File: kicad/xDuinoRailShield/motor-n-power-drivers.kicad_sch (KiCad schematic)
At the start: 3 parts, among them U5 ULN2003A, U6 ULN2003A, U8 DRV8872DDA

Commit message: More busses added
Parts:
- removed U6: ULN2003A, symbol Transistor_Array:ULN2003A
- renumbered U5 to U901, U8 to U902
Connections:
- net AUX1_AMP renamed AMP_AUX1
- net AUX2_AMP renamed AMP_AUX2
- net AUX3_AMP renamed AMP_AUX3
- net AUX4_AMP renamed AMP_AUX4
- net AUX5_AMP renamed AMP_AUX5
- net F0_BACKWARD renamed F01
- net F0_BACKWARD_AMP renamed AMP_F01
- net F0_FRONTWARD renamed F00
- net F0_FRONTWARD_AMP renamed AMP_F00
- net MOTOR+ renamed AMP_MOTOR0
- net MOTOR- renamed AMP_MOTOR1
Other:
- moved on the sheet: U901, U902

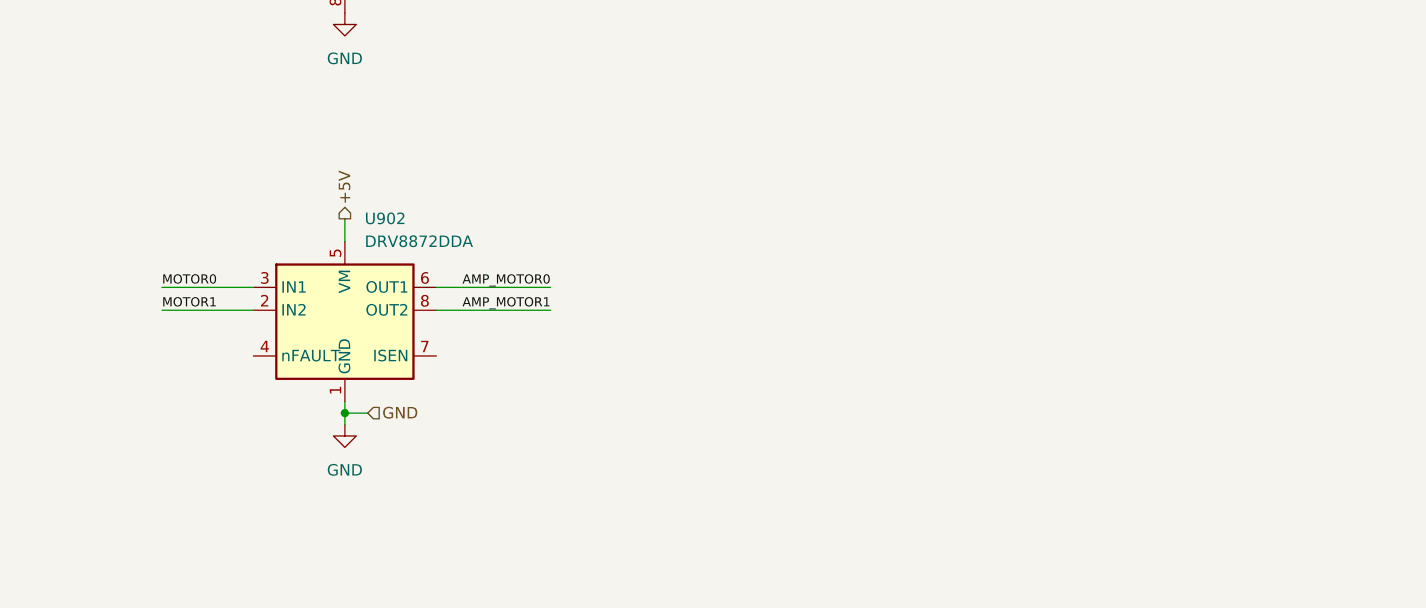
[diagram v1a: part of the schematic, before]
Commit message: Draft of loco decoder
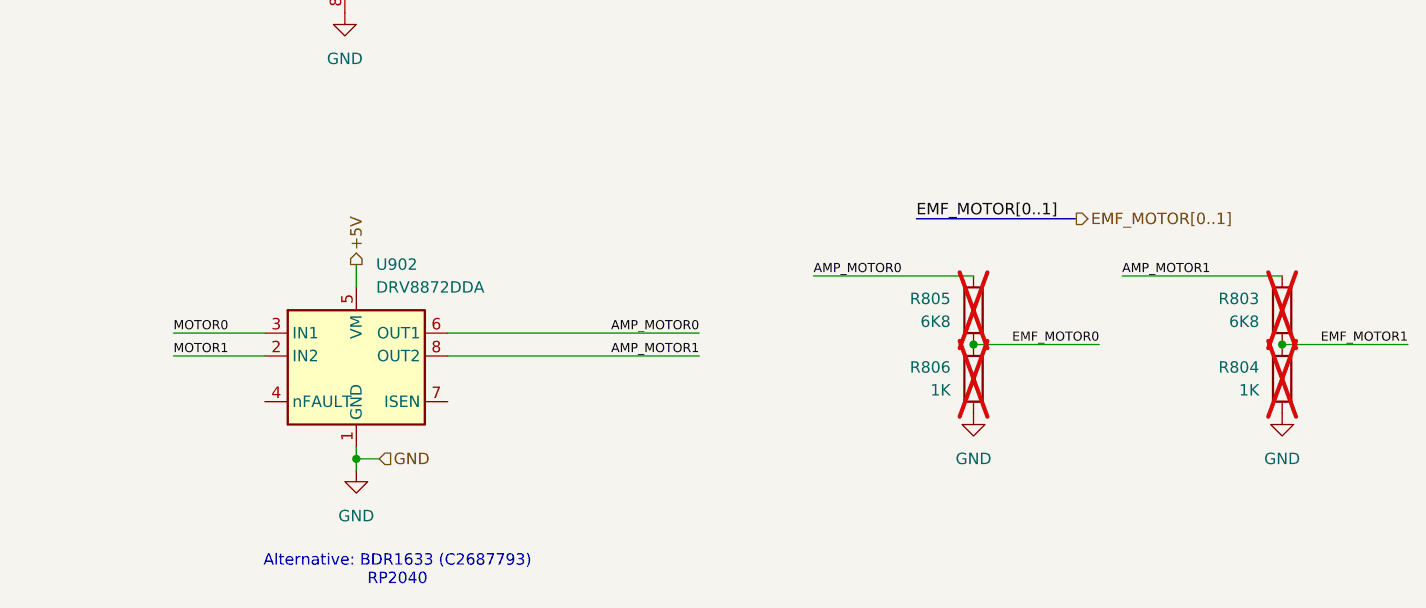
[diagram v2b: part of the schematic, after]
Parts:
- added R803, R805: 6K8, Resistor_SMD:R_0805_2012Metric_Pad1.20x1.40mm_HandSolder, symbol Device:R
- added R804, R806: 1K, Resistor_SMD:R_0805_2012Metric_Pad1.20x1.40mm_HandSolder, symbol Device:R
- U901: footprint (none) -> Package_SO:SOIC-16_4.55x10.3mm_P1.27mm; LCSC (none) -> C7512
- U902: LCSC (none) -> C114179
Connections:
- net AMP_MOTOR0: now also R805.1
- net AMP_MOTOR1: now also R803.1
- net GND: now also R804.2, R806.2
- new net EMF_MOTOR0: R805.2, R806.1
- new net EMF_MOTOR1: R803.2, R804.1
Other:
- note added: "Alternative: BDR1633 (C2687793) RP2040"
- moved on the sheet: U902

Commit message: A lot of fixes
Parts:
- removed U902: DRV8872DDA, Package_SO:Texas_HTSOP-8-1EP_3.9x4.9mm_P1.27mm_EP2.95x4.9mm_Mask2.4x3.1mm_ThermalVias, symbol Driver_Motor:DRV8872DDA
- added U801: BDR6133, BDR6133:BDR6133, symbol BDR6133:BDR6133
- added U802: DRV8872DDA, Package_SO:Texas_HTSOP-8-1EP_3.9x4.9mm_P1.27mm_EP2.95x4.9mm_Mask2.4x3.1mm_ThermalVias, symbol Driver_Motor:DRV8872DDA
- added U804: ULN2003A, Package_SO:SOIC-16_4.55x10.3mm_P1.27mm, symbol Transistor_Array:ULN2003A
- renumbered R805 to R801, R806 to R802, U901 to U803
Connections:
- net +5V: now also U801.2 (VCC), U802.5 (VM)
- net AMP_AUX2: no longer U803.13 (O4)
- net AMP_AUX3: no longer U803.12 (O5)
- net AMP_AUX4: no longer U803.11 (O6)
- net AMP_AUX5: no longer U803.10 (O7)
- net AMP_MOTOR0: now also U801.4 (OUTA), U802.6 (OUT1)
- net AMP_MOTOR1: now also U801.5 (OUTB), U802.8 (OUT2)
- net AUX2: no longer U803.4 (I4)
- net AUX3: no longer U803.5 (I5)
- net AUX4: no longer U803.6 (I6)
- net AUX5: no longer U803.7 (I7)
- net GND: now also U801.1 (GND), U802.1 (GND), U802.9 (GND), U804.8 (GND)
- net MOTOR0: now also U801.6 (INA), U802.3 (IN1)
- net MOTOR1: now also U801.7 (INB), U802.2 (IN2)
- net AMP_F00 renamed AMP_FUNC0
- net AMP_F01 renamed AMP_FUNC1
- net F00 renamed FUNC0
- net F01 renamed FUNC1
- new net AMP_AUX6: U804.16 (O1)
- new net AMP_AUX7: U804.15 (O2)
- new net AMP_AUX8: U804.14 (O3)
- new net AUX6: U804.1 (I1)
- new net AUX7: U804.2 (I2)
- new net AUX8: U804.3 (I3)
- new net U+: U801.3 (VM)
- no-connect marks 0 -> 28
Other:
- note added: "Motor Driver"
- note added: "Output Driver"
- note removed: "Alternative: BDR1633 (C2687793) RP2040"
- moved on the sheet: R801, R802, R803, R804, U803

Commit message: Final version
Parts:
- R801, R802, R803, R804: now fitted; now in the parts list
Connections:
- net AMP_AUX1: now also U803.15 (O2); no longer U803.14 (O3)
- net AMP_FUNC1: now also U803.14 (O3); no longer U803.15 (O2)
- net AUX1: now also U803.2 (I2); no longer U803.3 (I3)
- net FUNC1: now also U803.3 (I3); no longer U803.2 (I2)

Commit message: Refactoring & Sound
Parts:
- added Q801, Q802, Q803, Q804: 2N7002, Package_TO_SOT_SMD:SOT-23, symbol Transistor_FET:2N7002
- R801, R802, R803, R804: footprint Resistor_SMD:R_0805_2012Metric_Pad1.20x1.40mm_HandSolder -> Resistor_SMD:R_0402_1005Metric_Pad0.72x0.64mm_HandSolder
- U803: now not fitted; now left out of the parts list
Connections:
- net AMP_AUX1: now also Q803.3 (D)
- net AMP_AUX2: now also Q804.3 (D)
- net AMP_FUNC0: now also Q801.3 (D)
- net AMP_FUNC1: now also Q802.3 (D)
- net AUX1: now also Q803.1 (G)
- net AUX2: now also Q804.1 (G)
- net FUNC0: now also Q801.1 (G)
- net FUNC1: now also Q802.1 (G)
- net GND: now also Q801.2 (S), Q802.2 (S), Q803.2 (S), Q804.2 (S)

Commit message: More refactoring
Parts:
- Q801, Q802, Q803: LCSC (none) -> C8545
- R801, R803: value 6K8 -> 10k; LCSC C17772 -> C25744
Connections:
- net U+: now also U802.5 (VM)
- net +5V renamed +3V3
- net +3V3: no longer U802.5 (VM)
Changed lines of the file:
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@@
 	(wire
 		(pts
-			(xy 97.79 33.02) (xy 97.79 38.1)
+			(xy 97.79 31.75) (xy 97.79 38.1)
 		)
 		(stroke
@@
 		)
 	)
-	(hierarchical_label "+5V"
+	(hierarchical_label "+3V3"
 		(shape input)
 		(at 43.18 33.02 90)
@@
 		)
 	)
-	(hierarchical_label "+5V"
+	(hierarchical_label "U+"
 		(shape input)
-		(at 97.79 33.02 90)
+		(at 97.79 31.75 90)
 		(fields_autoplaced yes)
 		(effects
@@
 			)
 		)
-		(property "Value" "6K8"
+		(property "Value" "10k"
 			(at 41.91 110.4899 0)
 			(effects
@@
 			)
 		)
-		(property "LCSC" "C17772"
+		(property "LCSC" "C25744"
 			(at 44.45 109.22 0)
 			(effects
@@
 			)
 		)
+		(property "LCSC" "C8545"
+			(at 128.27 90.17 0)
+			(effects
+				(font
+					(size 1.27 1.27)
+				)
+				(hide yes)
+			)
+		)
 		(pin "3"
 		)
@@
 		)
 		(property "Description" "0.115A Id, 60V Vds, N-Channel MOSFET, SOT-23"
+			(at 88.9 90.17 0)
+			(effects
+				(font
+					(size 1.27 1.27)
+				)
+				(hide yes)
+			)
+		)
+		(property "LCSC" "C8545"
 			(at 88.9 90.17 0)
 			(effects
@@
 			)
 		)
-		(property "Value" "6K8"
+		(property "Value" "10k"
 			(at 41.91 85.0899 0)
 			(effects
@@
 			)
 		)
-		(property "LCSC" "C17772"
+		(property "LCSC" "C25744"
 			(at 44.45 83.82 0)
 			(effects
@@
 			(at 88.9 113.03 0)
 			(effects
+				(font
+					(size 1.27 1.27)
+				)
+				(hide yes)
+			)
+		)
+		(property "LCSC" "C8545"
+			(at 88.9 113.03 0)
+			(effects
